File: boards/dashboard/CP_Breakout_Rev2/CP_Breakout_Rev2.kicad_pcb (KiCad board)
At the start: 2 copper layers, 25.9 x 26.4 mm, 17 parts, among them J1 M06LOCK, J2 M02LOCK, J3 M06LOCK, U1 LM2936-3.3, U2 CP2120

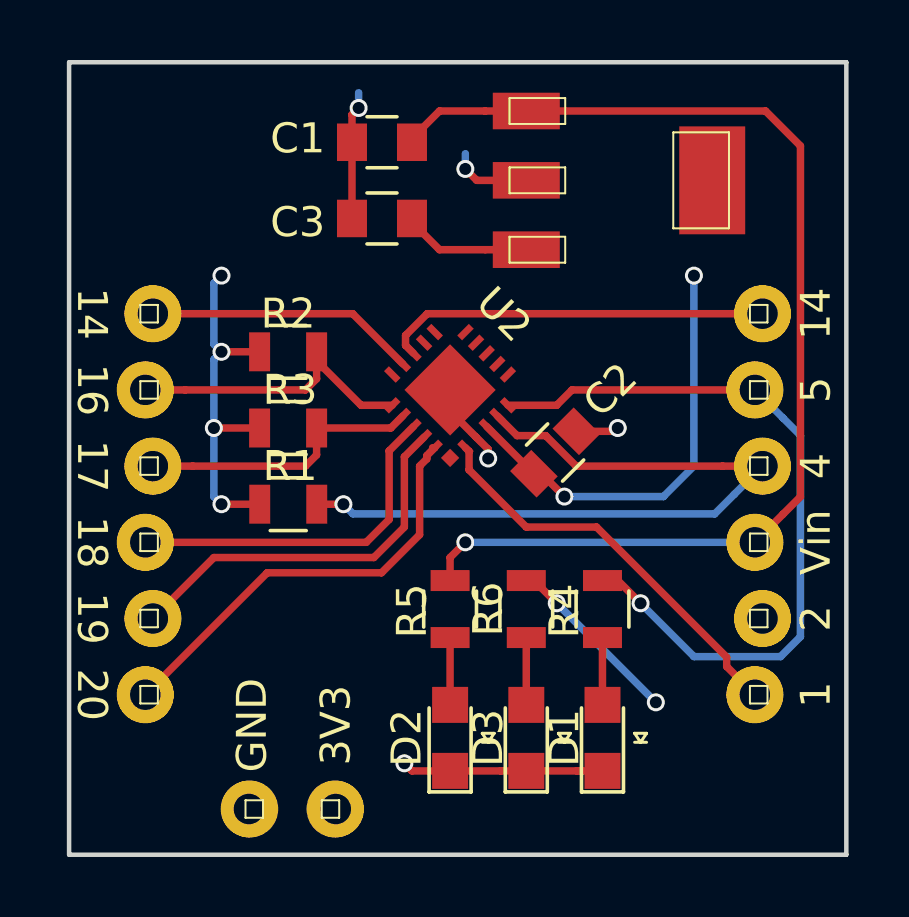
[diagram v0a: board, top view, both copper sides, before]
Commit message: Minor changes to CP2120 breakout
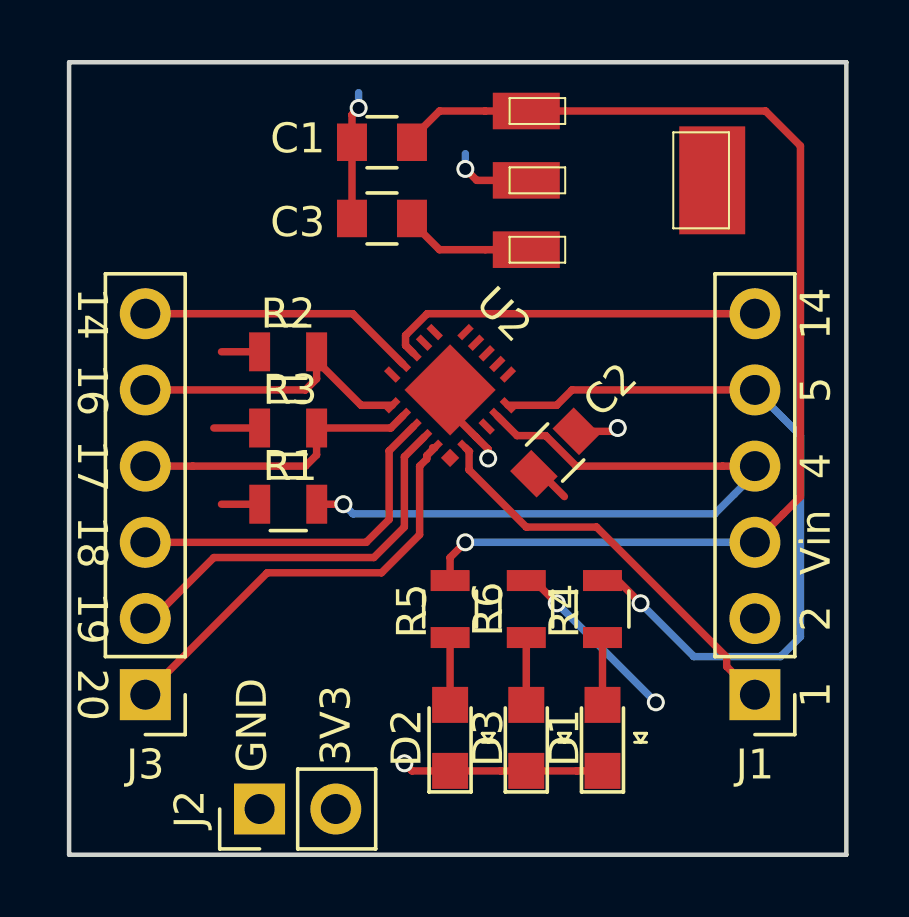
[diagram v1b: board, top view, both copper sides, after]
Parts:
- J1, J3: value M06LOCK -> Conn_01x06; footprint SparkFun-Connectors:1X06_LOCK -> Pin_Headers:Pin_Header_Straight_1x06_Pitch2.54mm
- J2: value M02LOCK -> Conn_01x02; footprint SparkFun-Connectors:1X02_LOCK -> Pin_Headers:Pin_Header_Straight_1x02_Pitch2.54mm
- moved J2 0.18 mm to (108.0, 147.3), turned to 90 degrees
- turned J1 to 180 degrees
- turned J3 to 180 degrees
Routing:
- net +3V3: track 37.1 -> 15.7 mm, vias 8 -> 2

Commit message: Revisions to CP2120 board files
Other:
- board text added: "13"
- board text added: "3.3V"
- board text added: "GPIO 0"
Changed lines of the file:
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@@
     (area 99.442381 122.352999 129.15762 152.017619)
     (thickness 1.6)
-    (drawings 18)
+    (drawings 21)
     (tracks 120)
     (zones 0)
@@
     (add_net VCC)
   )
+  (module footprints:LED_0805_OEM (layer F.Cu)
+    (at 114.3 144.95 90)
+    (descr "LED 0805 smd package")
+    (tags "LED led 0805 SMD smd SMT smt smdled SMDLED smtled SMTLED")
+    (attr smd)
+    (fp_text reference D2 (at 2.202 1.27 180) (layer F.SilkS)
+      (effects (font (size 0.635 0.635) (thickness 0.15)))
+    )
+    (fp_text value LED_0805 (at 0.508 2.032 90) (layer F.Fab) hide
+      (effects (font (size 1 1) (thickness 0.15)))
+    )
+    (fp_line (start -1.8 -0.7) (end -1.8 0.7) (layer F.SilkS) (width 0.12))
+    (fp_line (start -0.146 1.07) (end -0.146 1.47) (layer F.SilkS) (width 0.1))
+    (fp_line (start -0.146 1.27) (end 0.154 1.07) (layer F.SilkS) (width 0.1))
+    (fp_line (start 0.154 1.47) (end -0.146 1.27) (layer F.SilkS) (width 0.1))
+    (fp_line (start 0.154 1.07) (end 0.154 1.47) (layer F.SilkS) (width 0.1))
+    (fp_line (start 1 0.6) (end -1 0.6) (layer F.Fab) (width 0.1))
+    (fp_line (start 1 -0.6) (end 1 0.6) (layer F.Fab) (width 0.1))
+    (fp_line (start -1 -0.6) (end 1 -0.6) (layer F.Fab) (width 0.1))
+    (fp_line (start -1 0.6) (end -1 -0.6) (layer F.Fab) (width 0.1))
+    (fp_line (start -1.8 0.7) (end 1 0.7) (layer F.SilkS) (width 0.12))
+    (fp_line (start -1.8 -0.7) (end 1 -0.7) (layer F.SilkS) (width 0.12))
+    (fp_line (start 1.95 -0.85) (end 1.95 0.85) (layer F.CrtYd) (width 0.05))
+    (fp_line (start 1.95 0.85) (end -1.95 0.85) (layer F.CrtYd) (width 0.05))
+    (fp_line (start -1.95 0.85) (end -1.95 -0.85) (layer F.CrtYd) (width 0.05))
+    (fp_line (start -1.95 -0.85) (end 1.95 -0.85) (layer F.CrtYd) (width 0.05))
+    (pad 2 smd rect (at 1.1 0 270) (size 1.2 1.2) (layers F.Cu F.Paste F.Mask)
+      (net 5 "Net-(D2-Pad2)"))
+    (pad 1 smd rect (at -1.1 0 270) (size 1.2 1.2) (layers F.Cu F.Paste F.Mask)
+      (net 2 GND))
+    (model ${KISYS3DMOD}/LEDs.3dshapes/LED_0805.wrl
+      (at (xyz 0 0 0))
+      (scale (xyz 1 1 1))
+      (rotate (xyz 0 0 180))
+    )
+  )
   (module footprints:C_0805_OEM (layer F.Cu)
     (at 117.801107 135.436893 45)
@@
     (tags "LED led 0805 SMD smd SMT smt smdled SMDLED smtled SMTLED")
     (attr smd)
-    (fp_text reference D1 (at 0 -1.27 90) (layer F.SilkS)
-      (effects (font (size 1 1) (thickness 0.15)))
+    (fp_text reference D1 (at 2.202 1.27 180) (layer F.SilkS)
+      (effects (font (size 0.635 0.635) (thickness 0.15)))
     )
     (fp_text value LED_0805 (at 0.508 2.032 90) (layer F.Fab) hide
@@
   )
   (module footprints:LED_0805_OEM (layer F.Cu)
-    (at 114.3 144.95 90)
-    (descr "LED 0805 smd package")
-    (tags "LED led 0805 SMD smd SMT smt smdled SMDLED smtled SMTLED")
-    (attr smd)
-    (fp_text reference D2 (at 0 -1.45 90) (layer F.SilkS)
-      (effects (font (size 1 1) (thickness 0.15)))
-    )
-    (fp_text value LED_0805 (at 0.508 2.032 90) (layer F.Fab) hide
-      (effects (font (size 1 1) (thickness 0.15)))
-    )
-    (fp_line (start -1.8 -0.7) (end -1.8 0.7) (layer F.SilkS) (width 0.12))
-    (fp_line (start -0.146 1.07) (end -0.146 1.47) (layer F.SilkS) (width 0.1))
-    (fp_line (start -0.146 1.27) (end 0.154 1.07) (layer F.SilkS) (width 0.1))
-    (fp_line (start 0.154 1.47) (end -0.146 1.27) (layer F.SilkS) (width 0.1))
-    (fp_line (start 0.154 1.07) (end 0.154 1.47) (layer F.SilkS) (width 0.1))
-    (fp_line (start 1 0.6) (end -1 0.6) (layer F.Fab) (width 0.1))
-    (fp_line (start 1 -0.6) (end 1 0.6) (layer F.Fab) (width 0.1))
-    (fp_line (start -1 -0.6) (end 1 -0.6) (layer F.Fab) (width 0.1))
-    (fp_line (start -1 0.6) (end -1 -0.6) (layer F.Fab) (width 0.1))
-    (fp_line (start -1.8 0.7) (end 1 0.7) (layer F.SilkS) (width 0.12))
-    (fp_line (start -1.8 -0.7) (end 1 -0.7) (layer F.SilkS) (width 0.12))
-    (fp_line (start 1.95 -0.85) (end 1.95 0.85) (layer F.CrtYd) (width 0.05))
-    (fp_line (start 1.95 0.85) (end -1.95 0.85) (layer F.CrtYd) (width 0.05))
-    (fp_line (start -1.95 0.85) (end -1.95 -0.85) (layer F.CrtYd) (width 0.05))
-    (fp_line (start -1.95 -0.85) (end 1.95 -0.85) (layer F.CrtYd) (width 0.05))
-    (pad 2 smd rect (at 1.1 0 270) (size 1.2 1.2) (layers F.Cu F.Paste F.Mask)
-      (net 5 "Net-(D2-Pad2)"))
-    (pad 1 smd rect (at -1.1 0 270) (size 1.2 1.2) (layers F.Cu F.Paste F.Mask)
-      (net 2 GND))
-    (model ${KISYS3DMOD}/LEDs.3dshapes/LED_0805.wrl
-      (at (xyz 0 0 0))
-      (scale (xyz 1 1 1))
-      (rotate (xyz 0 0 180))
-    )
-  )
-  (module footprints:LED_0805_OEM (layer F.Cu)
     (at 116.84 144.95 90)
     (descr "LED 0805 smd package")
     (tags "LED led 0805 SMD smd SMT smt smdled SMDLED smtled SMTLED")
     (attr smd)
-    (fp_text reference D3 (at 0 -1.27 90) (layer F.SilkS)
-      (effects (font (size 1 1) (thickness 0.15)))
+    (fp_text reference D3 (at 2.202 1.27 180) (layer F.SilkS)
+      (effects (font (size 0.635 0.635) (thickness 0.15)))
     )
     (fp_text value LED_0805 (at 0.508 2.032 90) (layer F.Fab) hide
@@
     (tags "resistor 0805")
     (attr smd)
-    (fp_text reference R1 (at 0.061 -1.27) (layer F.SilkS)
-      (effects (font (size 1 1) (thickness 0.15)))
+    (fp_text reference R1 (at -2.225 0) (layer F.SilkS)
+      (effects (font (size 0.635 0.635) (thickness 0.15)))
     )
     (fp_text value 4.7k (at 0 1.75) (layer F.Fab) hide
@@
     (tags "resistor 0805")
     (attr smd)
-    (fp_text reference R2 (at 0 -1.27) (layer F.SilkS)
-      (effects (font (size 1 1) (thickness 0.15)))
+    (fp_text reference R2 (at -2.22 0) (layer F.SilkS)
+      (effects (font (size 0.635 0.635) (thickness 0.15)))
     )
     (fp_text value 4.7k (at 0 1.75) (layer F.Fab) hide
@@
     (tags "resistor 0805")
     (attr smd)
-    (fp_text reference R3 (at 0.066 -1.27) (layer F.SilkS)
-      (effects (font (size 1 1) (thickness 0.15)))
+    (fp_text reference R3 (at -2.22 0) (layer F.SilkS)
+      (effects (font (size 0.635 0.635) (thickness 0.15)))
     )
     (fp_text value 4.7k (at 0 1.75) (layer F.Fab) hide
@@
     (tags "resistor 0805")
     (attr smd)
-    (fp_text reference R4 (at 0.061 1.27 270) (layer F.SilkS)
-      (effects (font (size 1 1) (thickness 0.15)))
+    (fp_text reference R4 (at -2.225 0 360) (layer F.SilkS)
+      (effects (font (size 0.635 0.635) (thickness 0.15)))
     )
     (fp_text value R (at 0 1.75 270) (layer F.Fab) hide
@@
     (tags "resistor 0805")
     (attr smd)
-    (fp_text reference R5 (at 0.061 1.27 450) (layer F.SilkS)
-      (effects (font (size 1 1) (thickness 0.15)))
+    (fp_text reference R5 (at 0.061 1.524 270) (layer F.SilkS)
+      (effects (font (size 0.635 0.635) (thickness 0.15)))
     )
     (fp_text value R (at 0 1.75 270) (layer F.Fab) hide
@@
     (tags "resistor 0805")
     (attr smd)
-    (fp_text reference R6 (at 0 1.27 270) (layer F.SilkS)
-      (effects (font (size 1 1) (thickness 0.15)))
+    (fp_text reference R6 (at -2.225 0 360) (layer F.SilkS)
+      (effects (font (size 0.635 0.635) (thickness 0.15)))
     )
     (fp_text value R (at 0 1.75 270) (layer F.Fab) hide
@@
     )
   )
+  (gr_text "GPIO 0" (at 119.888 147.574) (layer F.SilkS)
+    (effects (font (size 0.635 0.635) (thickness 0.1524)))
+  )
+  (gr_text 3.3V (at 116.586 147.574) (layer F.SilkS)
+    (effects (font (size 0.635 0.635) (thickness 0.1524)))
+  )
+  (gr_text Vin (at 114.046 147.574) (layer F.SilkS)
+    (effects (font (size 0.635 0.635) (thickness 0.1524)))
+  )
   (gr_text Vin (at 126.492 138.43 90) (layer F.SilkS)
     (effects (font (size 1 1) (thickness 0.2)))
   )
-  (gr_text 14 (at 126.492 130.81 90) (layer F.SilkS)
+  (gr_text "13\n" (at 126.492 130.81 90) (layer F.SilkS)
     (effects (font (size 1 1) (thickness 0.2)))
   )
@@
   (gr_line (start 127.508 122.428) (end 101.6 122.428) (layer Edge.Cuts) (width 0.15))
   (gr_line (start 127.508 148.844) (end 127.508 122.428) (layer Edge.Cuts) (width 0.15))
-  (segment (start 124.8156 124.0536) (end 125.978801 125.216801) (width 0.25) (layer F.Cu) (net 1))
-  (segment (start 125.978801 125.216801) (end 125.978801 136.911199) (width 0.25) (layer F.Cu) (net 1))
-  (segment (start 125.978801 136.911199) (end 125.399799 137.490201) (width 0.25) (layer F.Cu) (net 1))
-  (segment (start 125.399799 137.490201) (end 124.46 138.43) (width 0.25) (layer F.Cu) (net 1))
-  (segment (start 116.84 124.0536) (end 124.8156 124.0536) (width 0.25) (layer F.Cu) (net 1))
+  (segment (start 124.8156 124.0536) (end 125.978801 125.216801) (width 0.635) (layer F.Cu) (net 1))
+  (segment (start 125.978801 125.216801) (end 125.978801 136.911199) (width 0.635) (layer F.Cu) (net 1))
+  (segment (start 125.978801 136.911199) (end 125.399799 137.490201) (width 0.635) (layer F.Cu) (net 1))
+  (segment (start 125.399799 137.490201) (end 124.46 138.43) (width 0.635) (layer F.Cu) (net 1))
+  (segment (start 116.84 124.0536) (end 124.8156 124.0536) (width 0.635) (layer F.Cu) (net 1))
   (segment (start 114.808 138.43) (end 124.46 138.43) (width 0.25) (layer B.Cu) (net 1))
   (segment (start 114.3 139.705) (end 114.3 138.938) (width 0.25) (layer F.Cu) (net 1))

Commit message: Progress
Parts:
- C3: value C_10uF -> C_0.1uF
- R1, R2, R3: value 4.7k -> 4.7kR
- R4, R5, R6: value R -> R_499
- U1: value LM2936-3.3 -> LM3480; footprint SparkFun-PowerIC:SOT223 -> TO_SOT_Packages_SMD:SOT-23
- moved C3 3.90 mm to (114.3, 124.5)
- moved C1 3.31 mm to (114.3, 127.5)
- moved J1 2.84 mm to (121.9, 142.2)
- moved U2 1.27 mm to (113.0, 133.3)
- moved J3 1.27 mm to (104.1, 142.2)
- moved C2 1.22 mm to (116.6, 135.4)
- moved U1 0.90 mm to (119.1, 126.0), turned to 0 degrees
- moved R1 0.70 mm to (108.2, 137.2)
- moved R2 0.70 mm to (108.2, 132.1)
- moved R3 0.70 mm to (108.2, 134.6)
- moved D3 0.25 mm to (116.6, 144.9)
- moved R6 0.25 mm to (116.6, 140.7)
- moved D1 0.25 mm to (119.1, 144.9)
- moved D2 0.25 mm to (114.0, 144.9)
- moved R4 0.25 mm to (119.1, 140.7)
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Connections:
- U1 pad 1: VCC -> +3V3
- U1 pad 2: GND -> VCC
- U1 pad 3: +3V3 -> GND
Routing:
- net VCC: track 38.9 -> 28.2 mm, vias 1 -> 0
- net +3V3: track 15.7 -> 5.34 mm, vias 2 -> 0
- net GPIO_0: track 25.2 -> 17.5 mm
- net RST: track 25.2 -> 19.5 mm, vias 1 -> 2
- net CS: track 11.9 -> 8.74 mm
- net MISO: track 14.5 -> 11.9 mm
- net MOSI: track 12.9 -> 10.6 mm
- net GND: track 17.9 -> 16.3 mm
- net SCL: track 10.2 -> 8.73 mm
- net SCLK: track 13.6 -> 12.4 mm, vias 0 -> 1
- net SDA: track 9.55 -> 8.72 mm
- net EINT: track 12.9 -> 12.4 mm
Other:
- board size 25.9 x 26.4 mm -> 23.1 x 26.4 mm
- net class Default: clearance 0.15 -> 0.1524; trace_width 0.25 -> 0.254; via_dia 0.6 -> 0.6096; via_drill 0.4 -> 0.3048
- rule trace_clearance: 0.15 -> 0.1524
- rule trace_min: 0.2 -> 0.1524
- rule via_min_drill: 0.3 -> 0.3048
- rule via_min_size: 0.4 -> 0.6096
- board text added: "Lauren Anfenson Olin Electric Motorsports CP2120 Breakout Rev 1"
